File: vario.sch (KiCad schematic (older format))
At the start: 177 parts, among them J10 Conn_01x06, J11 Conn_01x04, J12 Conn_01x04, J13 Conn_01x04, J14 Conn_01x03, J15 Conn_01x04, J16 Conn_01x06, J17 Conn_01x06, J18 Conn_01x04, J19 Conn_01x04, J2 Conn_01x02, J20 Conn_01x06, J21 Conn_Coaxial, J22 USB_B_Micro, J23 USB_B_Micro, J24 Micro_SD_Card_Det_Hirose_DM3AT, J3 6339167-3, J6 Conn_01x06, J7 Conn_01x04, J8 Conn_01x04, J9 Conn_01x02, Q1 AO3401A, SW1 SW_MEC_5E, U1 STM32F407VGTx, U10 AMS1117-3.3, U11 HSCMRRN001PD2A3, U12 MS5611-01BA, U13 MAX3232ECPWR, U14 BLE_HM-11, U15 USBLC6-2SC6, U16 USBLC6-2SC6, U17 AMS1117-3.3, U18 HAMMOND_1593W, U2 MP2359DJ-LF-Z, U3 MP2359DJ-LF-Z, U4 L3GD20, U5 MTi-1IMU, U6 FXOS8700, U7 MS5611-01BA, U8 NEO-M9N, U9 TCAN332DR, Y1 16MHz

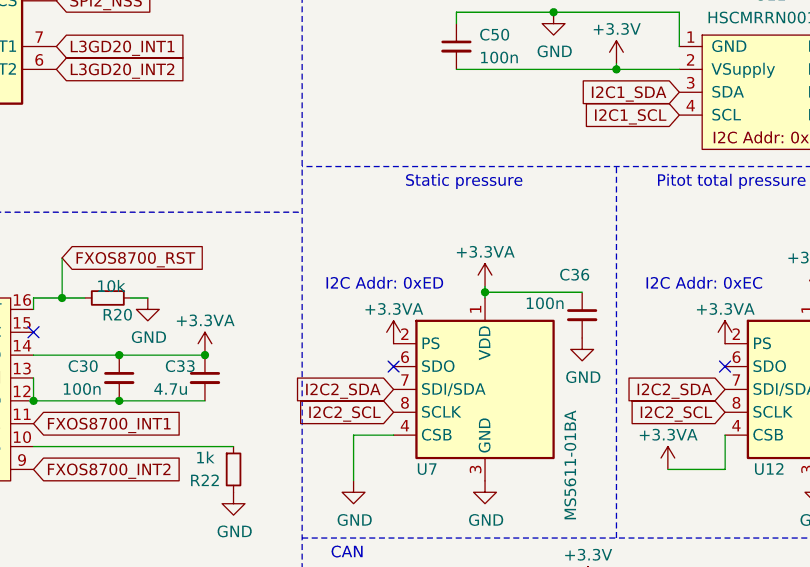
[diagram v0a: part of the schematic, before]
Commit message: again corrected a still wrong i2c address.
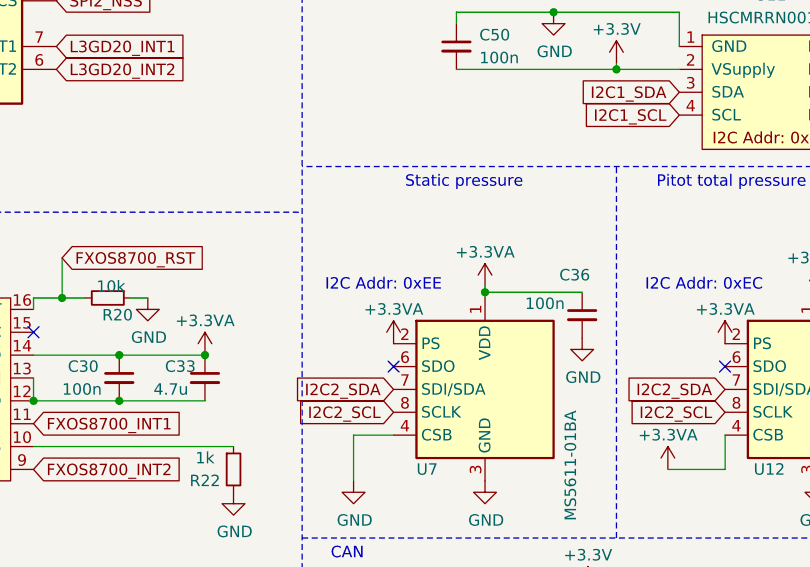
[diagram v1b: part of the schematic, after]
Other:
- note added: "I2C Addr: 0xEE"
- note removed: "I2C Addr: 0xED"
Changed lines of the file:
@@
 I2C Addr: 0xEC
 Text Notes 9850 6975 0    50   ~ 0
-I2C Addr: 0xED
+I2C Addr: 0xEE
 $Comp
 L Device:C_Small C38
